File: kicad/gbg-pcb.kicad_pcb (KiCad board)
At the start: 2 copper layers, 91.4 x 62.2 mm, 51 parts, among them J1 12 2.54mm pitch header pins, J11 weelye 7 or 9 pin connector, J2 Conn_01x02, J3 joystick, J4 speed knob, J5 TB005-762-02BE, J6 screw terminal, J7 1017491, J8 1017491, P1 rpi pico 1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

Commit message: layout
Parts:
- removed C4: 33uf, kicad libraries:CAP_KK-8x8_KEM
- removed HS1, HS3: Heatsink, kicad libraries:heatsink V2027B
- removed HS2, HS4: heatsink Tape, kicad libraries:tape_1
- added HSL1: Heatsink, kicad libraries:heatsink 375424B00034G, B.Cu at (81.7, 55.8)
- added HSR1: Heatsink, kicad libraries:heatsink 375424B00034G, B.Cu at (124.8, 55.8)
- added J10: 63900-1, kicad libraries:63900-1, F.Cu at (116.6, 40.5)
- added J9: 63900-1, kicad libraries:63900-1, F.Cu at (105.8, 40.5)
- moved C5 45.8 mm to (112.5, 72.4)
- moved D3 19.7 mm to (106.4, 66.8)
- moved R4 12.7 mm to (107.8, 57.8), turned to 180 degrees
- moved R9 7.04 mm to (137.5, 88.3)
- moved R1 2.92 mm to (133.3, 90.0)
- moved J5 2.79 mm to (113.1, 51.5)
- moved C7 2.35 mm to (137.4, 83.3), turned to -90 degrees
- moved R8 1.84 mm to (137.5, 78.6)
- moved R5 1.71 mm to (133.5, 86.6)
- moved C8 1.45 mm to (128.8, 78.2)
- moved C3 1.45 mm to (130.0, 83.3)
- moved C6 1.45 mm to (134.5, 78.7)
- moved D1 1.45 mm to (123.0, 78.2)
- moved U3 1.45 mm to (133.8, 82.6)
- moved Q1 0.74 mm to (112.4, 62.2)
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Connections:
- U1 pad 10: Net-(J7-Pad3) -> Net-(J7-Pad1)
- U1 pad 11: Net-(J7-Pad3) -> Net-(J7-Pad1)
- U1 pad 18: Net-(J7-Pad1) -> Net-(J7-Pad3)
- U1 pad 19: Net-(J7-Pad1) -> Net-(J7-Pad3)
- U1 pad 20: Net-(J7-Pad1) -> Net-(J7-Pad3)
- U1 pad 3: left_1 -> left_2
- U1 pad 4: left_2 -> left_1
- U1 pad 9: Net-(J7-Pad3) -> Net-(J7-Pad1)
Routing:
- net Net-(J3-Pin_1): track 0.00 -> 75.0 mm, vias 0 -> 4
- net GND: track 54.0 -> 19.8 mm, vias 63 -> 62
- net Net-(D3-K): track 10.1 -> 34.2 mm
- net Net-(Q2-G): track 1.54 -> 17.1 mm
- net 5V: track 58.3 -> 51.9 mm
- net +BATT: track 45.5 -> 50.2 mm
- net Net-(3V1-A): track 7.41 -> 4.49 mm
- net +3.3V: track 131.5 -> 134.5 mm
- net Net-(U3-FB): track 9.93 -> 11.2 mm
- net Net-(J3-Pin_3): track 76.1 -> 77.1 mm
- net Net-(D1-K): track 65.4 -> 64.8 mm
- net Net-(D3-A): track 5.83 -> 6.34 mm
- added copper zone on F.Cu, net Net-(J5-Pin_1)
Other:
- outline, holes or cut-outs redrawn
- board text added: "gobabygocarswithjoysticks@gmail.com"

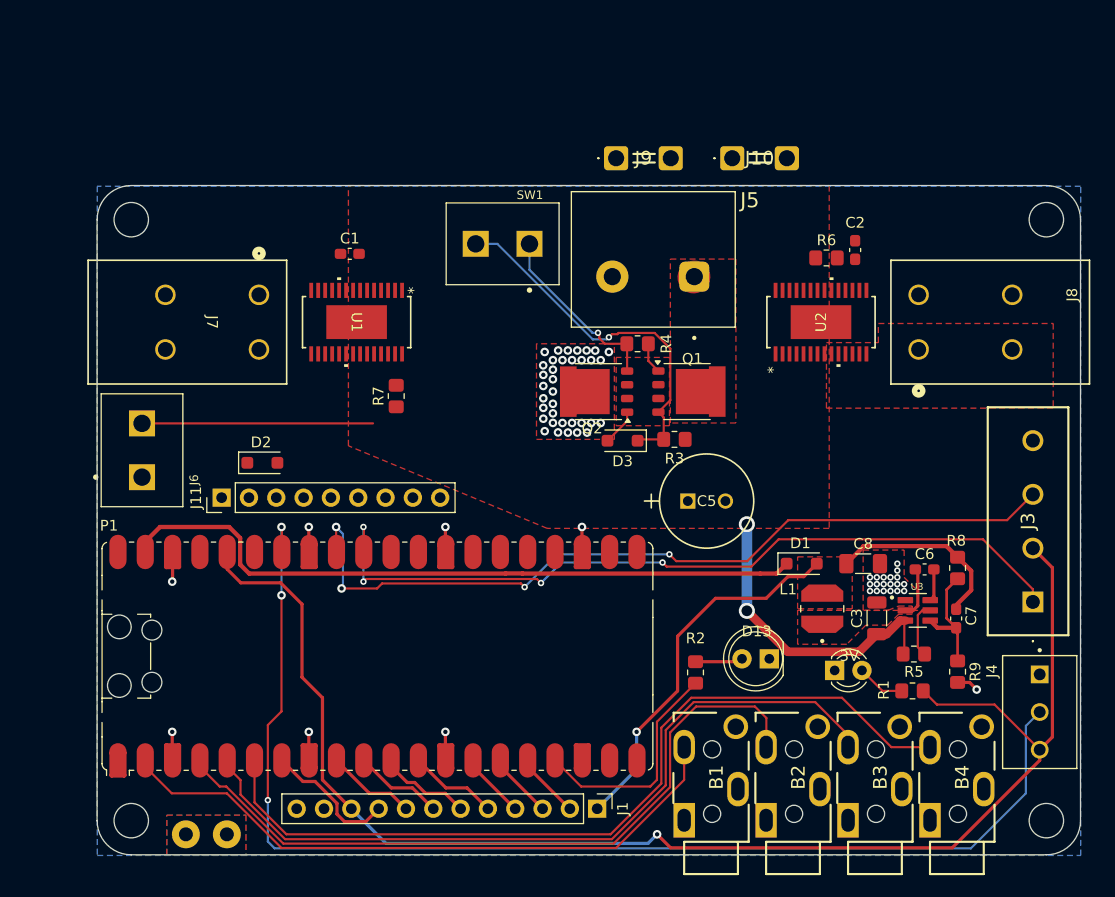
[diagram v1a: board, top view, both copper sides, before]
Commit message: draw traces
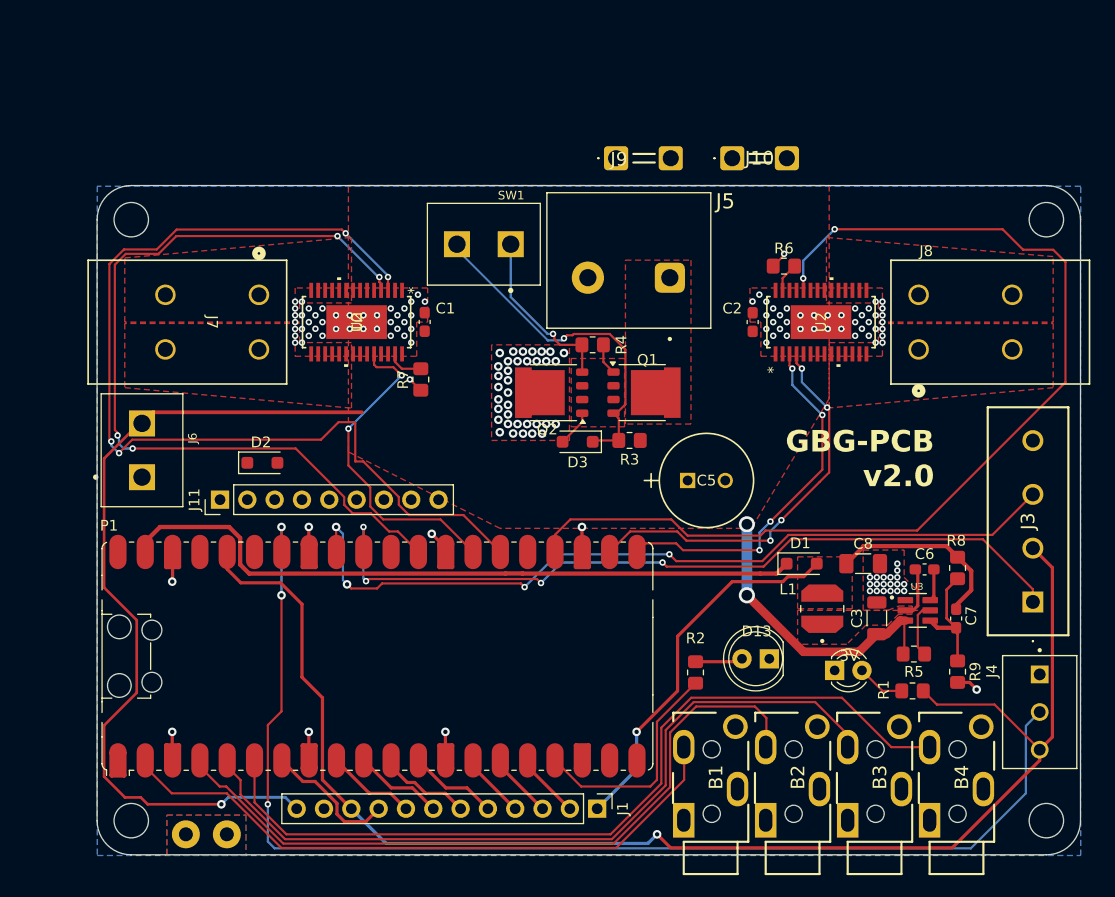
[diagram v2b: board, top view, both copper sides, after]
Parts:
- moved C2 11.6 mm to (118.5, 55.7)
- moved C1 9.41 mm to (88.0, 55.7), turned to 90 degrees
- moved Q2 4.18 mm to (100.0, 62.3)
- moved D3 4.18 mm to (102.2, 66.9)
- moved Q1 4.18 mm to (108.2, 62.3)
- moved R4 4.18 mm to (103.6, 57.9)
- moved R3 4.18 mm to (107.0, 66.8)
- moved R6 4.03 mm to (121.4, 50.5)
- moved R7 2.76 mm to (87.6, 61.1)
- moved J5 2.28 mm to (110.8, 51.6)
- moved C5 1.91 mm to (112.4, 70.5)
- moved SW1 1.75 mm to (96.0, 48.5)
- moved J11 0.24 mm to (69.0, 72.3)
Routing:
- net right_en: track 0.00 -> 97.0 mm, vias 0 -> 2
- net left_2: track 0.00 -> 92.6 mm, vias 0 -> 4
- net left_1: track 0.00 -> 77.8 mm, vias 0 -> 4
- net +BATT: track 50.2 -> 105.4 mm, vias 2 -> 3
- net right_2: track 0.00 -> 37.0 mm, vias 0 -> 4
- net right_1: track 0.00 -> 33.9 mm, vias 0 -> 4
- net left_en: track 0.00 -> 30.4 mm, vias 0 -> 2
- net Net-(U1-MODE): track 0.00 -> 3.41 mm
- net GND: track 19.8 -> 22.7 mm, vias 62 -> 146
- net Net-(U2-MODE): track 0.00 -> 2.72 mm
- net Net-(D3-K): track 34.2 -> 32.3 mm
- net Net-(Q2-G): track 17.1 -> 16.1 mm
- net Net-(J3-Pin_3): track 77.1 -> 76.5 mm
- added copper zone on F.Cu, net Net-(J7-Pad1)
- added copper zone on F.Cu, net Net-(J7-Pad3)
- added copper zone on F.Cu, net Net-(J8-Pad3)
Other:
- board text added: "GBG-PCB v2.0"
- board text added: "HSR1"
- board text added: "U2"

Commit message: layout
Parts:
- moved J8 0.32 mm to (142.9, 53.2)
- moved J7 0.25 mm to (63.6, 58.3)
- moved HSL1 0.17 mm to (81.5, 55.7)
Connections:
- net Net-(Q2-G) renamed switch
- J11 pad 1: unconnected-(J11-Pin_1-Pad1) -> +BATT
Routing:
- net switch: track 16.1 -> 39.0 mm
- net +BATT: track 105.4 -> 116.9 mm, vias 3 -> 4
- net left_2: track 92.6 -> 89.2 mm, vias 4 -> 2
- net left_1: track 77.8 -> 79.2 mm, vias 4 -> 2
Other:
- board text removed: "U2"

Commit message: v2
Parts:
- added J2: Conn_01x04, Connector_JST:JST_SH_BM04B-SRSS-TB_1x04-1MP_P1.00mm_Vertical, F.Cu at (134.3, 67.0)
- added NT5: NetTie_2, Jumper:SolderJumper-2_P1.3mm_Bridged_RoundedPad1.0x1.5mm, B.Cu at (83.7, 97.6)
- added NT6: NetTie_2, Jumper:SolderJumper-2_P1.3mm_Bridged_RoundedPad1.0x1.5mm, B.Cu at (86.2, 97.7)
- added NT7: NetTie_2, Jumper:SolderJumper-2_P1.3mm_Bridged_RoundedPad1.0x1.5mm, B.Cu at (88.8, 97.7)
- added NT8: NetTie_2, Jumper:SolderJumper-2_P1.3mm_Bridged_RoundedPad1.0x1.5mm, B.Cu at (91.3, 97.7)
- added R10: 220k, kicad libraries:YC248-JR-072K2L, F.Cu at (71.8, 101.1)
- added U4: TLA2024IRUGR, kicad libraries:IC_TLA2024IRUGR, F.Cu at (128.4, 71.2)
- J11: value weelye 7 or 9 pin connector -> Conn_01x10_Pin; footprint Connector_PinHeader_2.54mm:PinHeader_1x09_P2.54mm_Vertical -> Connector_PinHeader_2.54mm:PinHeader_1x10_P2.54mm_Vertical
- moved J2 88.1 mm to (131.8, 45.1), turned to 180 degrees
- moved J10 18.8 mm to (108.2, 57.3), turned to 90 degrees
- moved J9 11.3 mm to (116.1, 45.3), turned to 180 degrees
- moved D2 5.82 mm to (68.2, 65.4)
- moved J11 2.04 mm to (69.1, 70.2)
- moved J3 1.94 mm to (142.6, 81.6)
- moved C7 1.69 mm to (135.8, 83.7)
- moved C3 1.46 mm to (128.6, 83.7)
- moved C6 1.46 mm to (133.1, 79.1)
- moved C8 1.46 mm to (127.3, 78.6)
- moved L1 1.46 mm to (123.5, 82.8)
- moved R8 1.46 mm to (136.1, 79.0)
- moved U3 1.46 mm to (132.4, 82.9)
- moved D1 1.46 mm to (121.6, 78.6)
- moved D13 1.05 mm to (119.0, 87.2)
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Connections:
- D2 pad 1: unconnected-(D2-K-Pad1) -> +BATT
- D2 pad 2: unconnected-(D2-A-Pad2) -> Net-(D2-A)
- J10 pad 1: Net-(J5-Pin_1) -> bat-
- J10 pad 2: Net-(J5-Pin_1) -> bat-
- J11 pad 2: unconnected-(J11-Pin_2-Pad2) -> switch
- J11 pad 3: unconnected-(J11-Pin_3-Pad3) -> Net-(D2-A)
- J11 pad 4: unconnected-(J11-Pin_4-Pad4) -> bat-
- J11 pad 5: unconnected-(J11-Pin_5-Pad5) -> GND
- J5 pad 1: Net-(J5-Pin_1) -> bat-
- P1 pad 10: Net-(J1-Pin_7) -> Net-(P1-GP7)
- P1 pad 11: Net-(J1-Pin_6) -> Net-(P1-GP8)
- P1 pad 19: unconnected-(P1-GP14-Pad19) -> sda
- P1 pad 20: unconnected-(P1-GP15-Pad20) -> scl
- P1 pad 7: Net-(J1-Pin_9) -> Net-(P1-GP5)
- P1 pad 9: Net-(J1-Pin_8) -> Net-(P1-GP6)
- Q1 pad 5: Net-(J5-Pin_1) -> bat-
- SW1 pad 1: switch -> Net-(D3-K)
- SW1 pad 2: Net-(D3-K) -> switch
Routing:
- net bat-: track 0.00 -> 103.3 mm, vias 0 -> 2
- net switch: track 39.0 -> 91.3 mm, vias 1 -> 2
- net Net-(P1-GP8): track 0.00 -> 25.0 mm, vias 0 -> 1
- net Net-(P1-GP7): track 0.00 -> 24.1 mm, vias 0 -> 1
- net Net-(P1-GP6): track 0.00 -> 22.8 mm, vias 0 -> 1
- net Net-(P1-GP5): track 0.00 -> 21.8 mm, vias 0 -> 1
- net Net-(J1-Pin_8): track 8.32 -> 29.4 mm, vias 0 -> 1
- net +3.3V: track 134.5 -> 150.6 mm, vias 1 -> 3
- net Net-(J1-Pin_6): track 8.65 -> 23.6 mm, vias 0 -> 2
- net Net-(J1-Pin_7): track 8.32 -> 22.2 mm, vias 0 -> 2
- net Net-(J4-Pin_2): track 113.1 -> 100.2 mm
- net GND: track 22.7 -> 35.3 mm
- net Net-(J1-Pin_9): track 12.4 -> 23.3 mm, vias 0 -> 1
- net +BATT: track 116.9 -> 127.4 mm
- net bt4: track 78.2 -> 86.2 mm
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- added copper zone on F.Cu, net bat-
- removed copper zone on F.Cu, net Net-(J5-Pin_1)
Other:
- board text added: "3V"
- board text added: "3V A28 gnd"
- board text added: "GND"
- board text added: "LEFT"
- board text added: "RIGHT"
- board text added: "X"
- board text added: "Y"
- board text added: "bat+ sw chg bat- GND"
- board text added: "gobabygocarswithjoysticks@gmail.com https://github.com/gobabygocarswithjoysticks/gbg-pcb"
- board text added: "speed"
- board text added: "voltage dividers"
- board text removed: "HSR1"
- board text removed: "gobabygocarswithjoysticks@gmail.com"

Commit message: adjust layout
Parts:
- removed J10, J9: 63900-1, kicad libraries:63900-1
- added C4: 0.1uF, Capacitor_SMD:C_0603_1608Metric_Pad1.08x0.95mm_HandSolder, F.Cu at (125.2, 74.0)
- added NT1: NetTie_3, Jumper:SolderJumper-3_P1.3mm_Bridged12_RoundedPad1.0x1.5mm, B.Cu at (130.2, 71.8)
- added R11: 604, Resistor_SMD:R_0805_2012Metric_Pad1.20x1.40mm_HandSolder, F.Cu at (126.2, 71.0)
- added R12: 220, Resistor_SMD:R_0805_2012Metric_Pad1.20x1.40mm_HandSolder, F.Cu at (129.5, 64.5)
- added R13: 100k, Resistor_SMD:R_0805_2012Metric_Pad1.20x1.40mm_HandSolder, F.Cu at (123.0, 71.7)
- added R14: 13.7k, Resistor_SMD:R_0805_2012Metric_Pad1.20x1.40mm_HandSolder, F.Cu at (126.6, 66.8)
- added TP0: TestPoint, TestPoint:TestPoint_THTPad_D2.0mm_Drill1.0mm, F.Cu at (129.5, 68.0)
- added U5: D78B05T, RBT05W24S05, kicad libraries:D78B05T-1.0, F.Cu at (118.7, 84.4)
- moved D1 10.5 mm to (111.5, 81.5), turned to -90 degrees
- moved D13 6.97 mm to (125.8, 88.7)
- moved R1 6.91 mm to (140.2, 89.5), turned to -90 degrees
- moved 3V1 2.75 mm to (128.9, 88.6)
- moved C5 2.17 mm to (114.2, 69.2)
- moved R2 1.51 mm to (111.7, 88.1)
- moved R5 1.44 mm to (134.0, 88.0), turned to -90 degrees
- moved U4 1.42 mm to (129.8, 71.3), turned to 180 degrees
- moved R9 1.16 mm to (136.4, 88.0)
- moved J2 0.80 mm to (134.3, 67.8), turned to 90 degrees
- moved R7 0.53 mm to (87.6, 60.4)
- moved C7 0.46 mm to (135.8, 83.2)
- moved HSL1 0.21 mm to (81.4, 55.7)
- moved R6 0.13 mm to (121.4, 50.4)
- moved J7 0.06 mm to (63.6, 58.3)
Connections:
- J2 pad 1: unconnected-(J2-Pin_1-Pad1) -> GND
- J2 pad 2: unconnected-(J2-Pin_2-Pad2) -> +3.3V
- J2 pad 3: unconnected-(J2-Pin_3-Pad3) -> sda
- J2 pad 4: unconnected-(J2-Pin_4-Pad4) -> scl
- J2 pad MP: (no net) -> unconnected-(J2-Shield-PadMP)_1
- U1 pad 25: unconnected-(U1-IPROPI-Pad25) -> left_ipropi
- U2 pad 25: unconnected-(U2-IPROPI-Pad25) -> right_ipropi
- U4 pad 1: unconnected-(U4-ADDR-Pad1) -> Net-(U4-ADDR)
- U4 pad 3: unconnected-(U4-GND-Pad3) -> GND
- U4 pad 4: unconnected-(U4-AIN0-Pad4) -> Net-(U4-AIN0)
- U4 pad 5: unconnected-(U4-AIN1-Pad5) -> right_ipropi
- U4 pad 6: unconnected-(U4-AIN2-Pad6) -> Net-(U4-AIN2)
- U4 pad 7: unconnected-(U4-AIN3-Pad7) -> left_ipropi
- U4 pad 8: unconnected-(U4-VDD-Pad8) -> +3.3V
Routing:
- net left_ipropi: track 0.00 -> 79.7 mm, vias 0 -> 6
- net right_ipropi: track 0.00 -> 72.3 mm, vias 0 -> 2
- net sda: track 0.00 -> 55.0 mm, vias 0 -> 4
- net scl: track 0.00 -> 53.2 mm, vias 0 -> 6
- net +3.3V: track 150.6 -> 178.7 mm
- net +BATT: track 127.4 -> 138.7 mm
- net Net-(D13-A): track 3.32 -> 13.0 mm
- net GND: track 35.3 -> 44.4 mm, vias 146 -> 131
- net Net-(D1-K): track 63.2 -> 54.6 mm
- net Net-(U4-AIN2): track 0.00 -> 8.12 mm
- net Net-(3V1-A): track 4.38 -> 9.61 mm
- net Net-(U3-EN): track 5.33 -> 9.70 mm
- net 5V: track 52.1 -> 55.6 mm
- net Net-(U4-AIN0): track 0.00 -> 2.94 mm
- net Net-(J3-Pin_3): track 76.2 -> 78.2 mm
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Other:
- board text added: "0 B1-1 GND B2-2 B3-3 B4-4 5 GND 6 7 8 9 GND 10 11 12 D13 GND 14 15"
- board text added: "5v"
- board text added: "BATT G 3V 5 6 7 8 9 10 11 12 5v"
- board text added: "G"
- board text added: "GBG-PCB"
- board text added: "I2C"
- board text added: "SDA SCL"
- board text added: "VBUS 5V GND EN 3V3 VREF A28-A GND A27-Y A26-X RUN 22-L1 GND 21-Len 20-L2 19 18-Ren GND 17-R2 16-R1"
- board text added: "bat"
- board text added: "cut to activate voltage dividers"
- board text added: "gobabygocarswithjoysticks@gmail.com github.com/gobabygocarswithjoysticks/gbg-pcb"
- board text added: "v2.0"
- board text removed: "GBG-PCB v2.0"
- board text removed: "gobabygocarswithjoysticks@gmail.com https://github.com/gobabygocarswithjoysticks/gbg-pcb"
- board text removed: "voltage dividers"

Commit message: adjust layout
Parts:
- moved R13 1.05 mm to (123.8, 71.0), turned to 90 degrees
- moved TP0 0.89 mm to (130.3, 67.5)
- moved 3V1 0.30 mm to (129.2, 88.6)
- moved D13 0.10 mm to (125.9, 88.7)
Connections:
- P1 pad 18: unconnected-(P1-GND__3-Pad18) -> GND
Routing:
- net GND: track 44.4 -> 47.3 mm, vias 131 -> 132
- net +BATT: track 138.7 -> 140.1 mm
- net Net-(U4-AIN2): track 8.12 -> 7.58 mm
- net left_ipropi: track 79.7 -> 80.2 mm

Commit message: adjust layout
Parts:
- moved J2 0.14 mm to (134.3, 67.7)
- renumbered J2 to JGND2
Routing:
- net +BATT: track 140.1 -> 135.5 mm
- net GND: track 47.3 -> 49.0 mm
- net Net-(P1-GP6): track 22.8 -> 21.8 mm
- net +3.3V: track 178.7 -> 179.5 mm, vias 3 -> 4
- net Net-(J1-Pin_8): track 29.4 -> 30.1 mm
- net scl: track 53.2 -> 52.8 mm, vias 6 -> 4
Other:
- board text added: "0 GND B2-2 B3-3 B4-4 5 GND 6 7 8 9 GND 10 11 12 D13 GND 14 15"
- board text added: "5V GND EN 3V3 VREF A28-A GND A27-Y A26-X RUN 22-L1 GND 21-Len 20-L2 19 18-Ren GND 17-R2 16-R1"
- board text added: "B1-1"
- board text added: "VBUS"
- board text removed: "0 B1-1 GND B2-2 B3-3 B4-4 5 GND 6 7 8 9 GND 10 11 12 D13 GND 14 15"
- board text removed: "VBUS 5V GND EN 3V3 VREF A28-A GND A27-Y A26-X RUN 22-L1 GND 21-Len 20-L2 19 18-Ren GND 17-R2 16-R1"

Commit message: fix script
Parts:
- added TP1: TestPoint, TestPoint:TestPoint_Pad_D2.0mm, B.Cu at (81.8, 82.1)
- added TP2: TestPoint, TestPoint:TestPoint_Pad_D2.0mm, B.Cu at (135.3, 64.8)
- TP0: value TestPoint -> TP0
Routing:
- net left_ipropi: track 80.2 -> 81.7 mm
- net right_ipropi: track 72.2 -> 73.6 mm, vias 2 -> 3
- net GND: track 49.0 -> 49.8 mm
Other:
- board text added: "1"
- board text added: "21"
